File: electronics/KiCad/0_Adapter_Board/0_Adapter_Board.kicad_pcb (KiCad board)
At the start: 2 copper layers, 70 x 50 mm, 19 parts, among them J1 Conn_01x10, J2 Conn_01x10, J3 Conn_01x04, J4 Conn_01x04, J5 Conn_01x03, M1 MountingHole_3.2mm_M3_ISO7380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

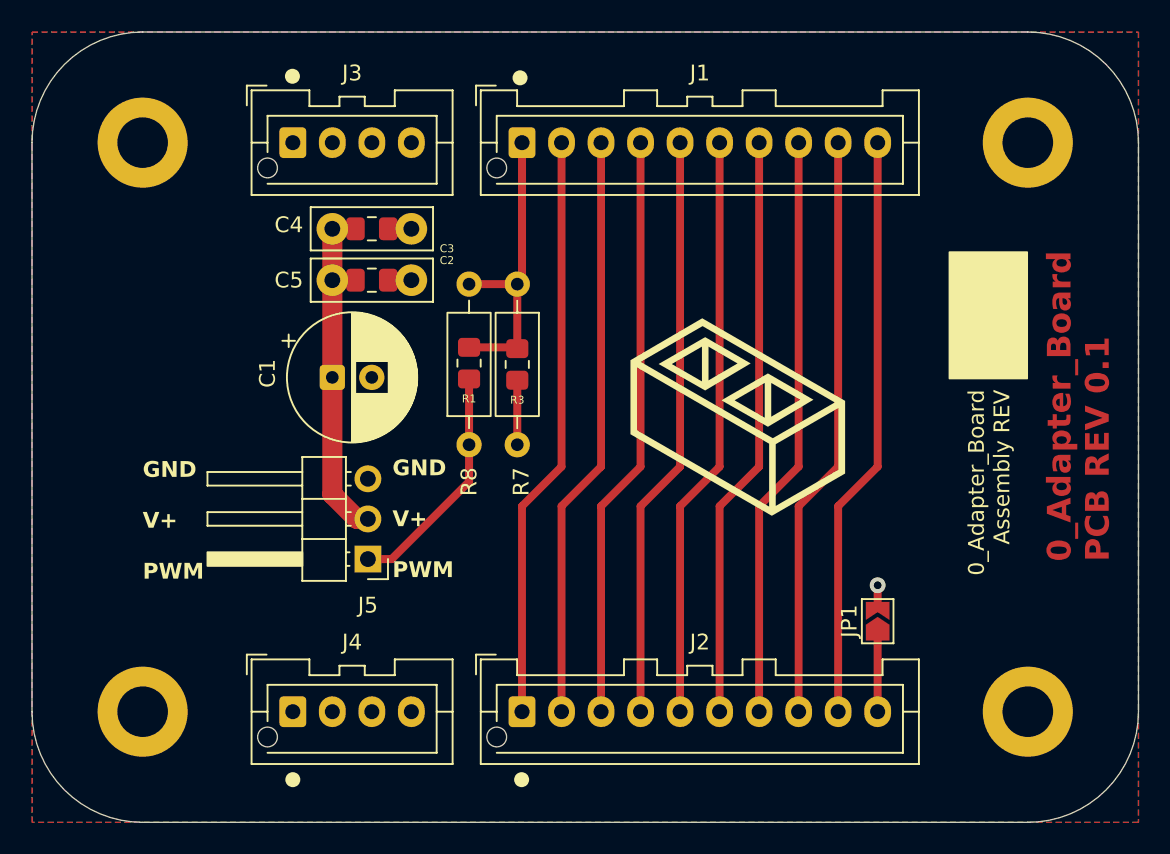
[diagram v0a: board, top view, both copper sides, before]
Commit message: Merge board v1.3 into main (clean-clone fixups, generated files trimmed to main level) (#289)
* Initial start to updates

Removed motor pages, updated Q2,Q3, Cleaned up power module connections.

- Still need to correct routing for these updates.

* PCA Update

Updated PCA to have level shifter for I2C lines and external oscillator for precision. Corrected Power to pull from 12V.

* Removed old circuits from PCB

Removed all unused traces

* Mid work update

Lots of rework on the SCH and PCB. Checkpoint.

* Updated with more layout

Compelted PCA on board.

* adding libraries

* REV0.9 for review

Took care of all open items on the electronics PCB except for the driver resistor addresses.

* Updates Just prior to Ordering V1.0 PCBs

Updates Just prior to Ordering V1.0 PCBs

* Updates to push to V1.0

Updates to push to V1.0

* Updates to push to V1.0 missing saves. . .

Updates to push to V1.0 missing saves. . .

* Correcting Part rotation for JLCPCB

Several parts needed the "FT Rotation Offset" parameter added to correct for part orientation for JLCPCB order.

* All orientations corrected

* latest update

* Updated to reflect V1.0 of layer board as well

Updated for initial orders with PCA module populated. Also updated to layer boards for flex cables.

* Updated data and notes

* Corrected SCH for power sequence issue

5V to Vsys for all powered items.
Correction of the PCA9306 power pins.
Added decoupling to oscillator and PCA9306.

* Updated for changes to the SCH items

Updated PCB to include all changed from the SCH.

* Updated rules to correct errors

Cleaned up rules a bit to prevent false errors.

* Started work on silk update

Slowly started work on silk update.

* Corrected the 10k to 1k for connecting resistors

R1 got fixed for the correct 1k instead of 10k for UART1

* Updated Silk on PCB

Added notes for describing the pins better in the silk layer.

* Updated REV to 1.3 to reflect changes

* Updated with Version 1.3

* KiCad: make the v1.3 project 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
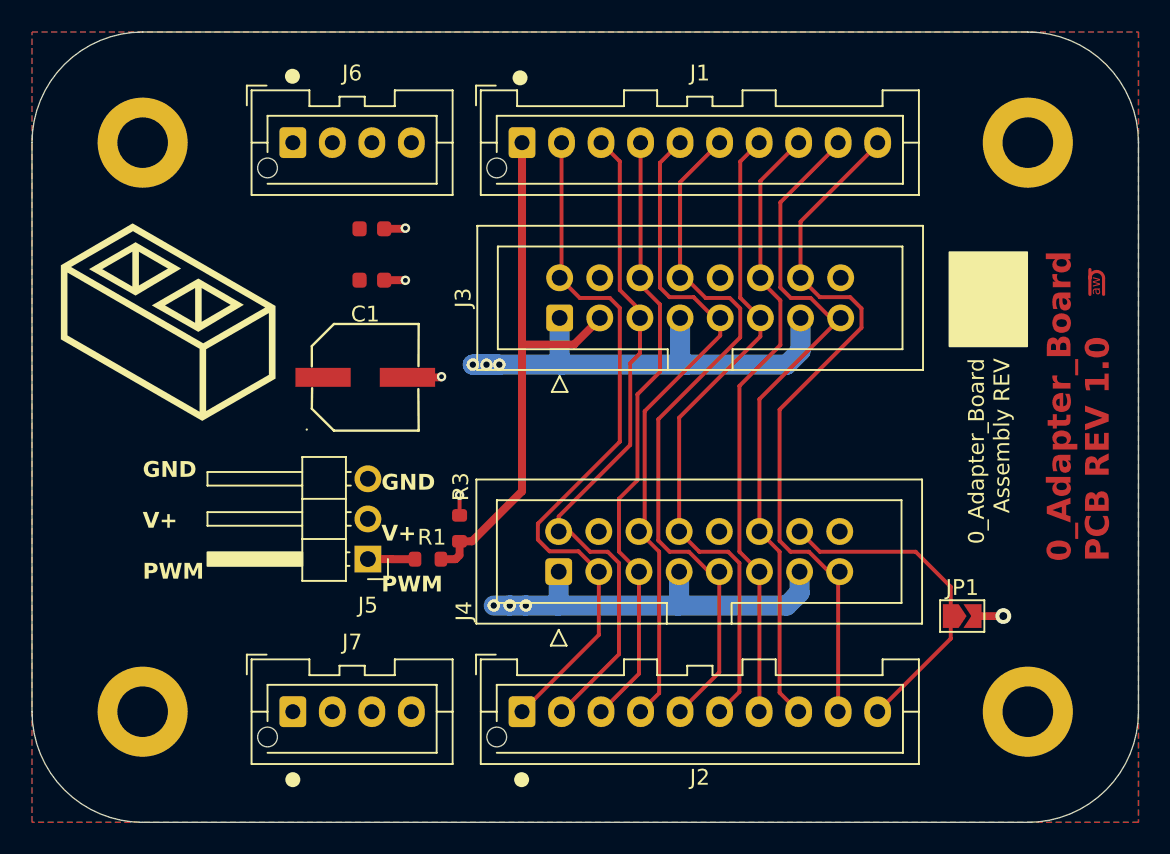
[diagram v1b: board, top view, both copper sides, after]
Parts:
- removed C4: 0.1uF, Capacitor_THT:C_Disc_D7.5mm_W2.5mm_P5.00mm
- removed C5: 1uF, Capacitor_THT:C_Disc_D7.5mm_W2.5mm_P5.00mm
- removed R7: 10k, Resistor_THT:R_Axial_DIN0207_L6.3mm_D2.5mm_P10.16mm_Horizontal
- removed R8: 0, Resistor_THT:R_Axial_DIN0207_L6.3mm_D2.5mm_P10.16mm_Horizontal
- added J6: Conn_01x04, Connector_JST:JST_XA_B04B-XASK-1-A_1x04_P2.50mm_Vertical, F.Cu at (76.5, 57.0)
- added J7: Conn_01x04, Connector_JST:JST_XA_B04B-XASK-1-A_1x04_P2.50mm_Vertical, F.Cu at (76.5, 93.0)
- added JAW: Maker's Mark, JAW:JAW, F.Cu at (127.4, 65.9)
- C1: value Filter Cap -> 100uF; footprint Capacitor_THT:CP_Radial_D8.0mm_P2.50mm -> EasyEDA:CAP-SMD_BD6.3-L6.6-W6.6-LS7.4-FD
- C2: footprint Capacitor_SMD:C_0805_2012Metric_Pad1.18x1.45mm_HandSolder -> PCM_JLCPCB:C_0603
- C3: value 0.1uF -> 100nF; footprint Capacitor_SMD:C_0805_2012Metric_Pad1.18x1.45mm_HandSolder -> PCM_JLCPCB:C_0603
- J3, J4: value Conn_01x04 -> Conn_02x08_Odd_Even; footprint Connector_JST:JST_XA_B04B-XASK-1-A_1x04_P2.50mm_Vertical -> Connector_IDC:IDC-Header_2x08_P2.54mm_Vertical
- R1: value 0 -> 0Ω; footprint Resistor_SMD:R_0805_2012Metric_Pad1.20x1.40mm_HandSolder -> PCM_JLCPCB:R_0603
- R3: value 10k -> 10kΩ; footprint Resistor_SMD:R_0805_2012Metric_Pad1.20x1.40mm_HandSolder -> PCM_JLCPCB:R_0603
- moved J3 20.2 mm to (93.4, 68.1), turned to 90 degrees
- moved J4 19.0 mm to (93.3, 84.1), turned to 90 degrees
- moved R1 12.7 mm to (85.0, 83.3), turned to 180 degrees
- moved R3 11.0 mm to (87.0, 81.4), turned to 90 degrees
- moved JP1 5.36 mm to (118.8, 87.0), turned to 0 degrees
- moved C2 3.25 mm to (81.5, 62.5)
- moved C3 3.25 mm to (81.5, 65.7)
- moved C1 2.08 mm to (81.1, 71.8)
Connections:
- C1 pad 1: +5V -> +ServoV
- C2 pad 1: +5V -> +ServoV
- C3 pad 1: +5V -> +ServoV
- J1 pad 1: /PWM_Signal -> /PWM_0
- J1 pad 10: Net-(J1-Pin_10) -> /PWM_9
- J1 pad 2: Net-(J1-Pin_2) -> /PWM_1
- J1 pad 3: Net-(J1-Pin_3) -> /PWM_2
- J1 pad 4: Net-(J1-Pin_4) -> /PWM_3
- J1 pad 5: Net-(J1-Pin_5) -> /PWM_4
- J1 pad 6: Net-(J1-Pin_6) -> /PWM_5
- J1 pad 7: Net-(J1-Pin_7) -> /PWM_6
- J1 pad 8: Net-(J1-Pin_8) -> /PWM_7
- J1 pad 9: Net-(J1-Pin_9) -> /PWM_8
- J2 pad 1: Net-(J1-Pin_2) -> /PWM_1
- J2 pad 10: Net-(J2-Pin_10) -> /Dead_Pin
- J2 pad 2: Net-(J1-Pin_3) -> /PWM_2
- J2 pad 3: Net-(J1-Pin_4) -> /PWM_3
- J2 pad 4: Net-(J1-Pin_5) -> /PWM_4
- J2 pad 5: Net-(J1-Pin_6) -> /PWM_5
- J2 pad 6: Net-(J1-Pin_7) -> /PWM_6
- J2 pad 7: Net-(J1-Pin_8) -> /PWM_7
- J2 pad 8: Net-(J1-Pin_9) -> /PWM_8
- J2 pad 9: Net-(J1-Pin_10) -> /PWM_9
- J3 pad 1: +5V -> +ServoV
- J3 pad 2: +5V -> /PWM_1
- J3 pad 3: GND -> /PWM_0
- J4 pad 1: +5V -> +ServoV
- J4 pad 2: +5V -> /PWM_2
- J4 pad 3: GND -> /PWM_1
- J5 pad 1: /Pin1_J5 -> /PWM_Signal
- J5 pad 2: +5V -> +ServoV
- JP1 pad 1: Net-(J2-Pin_10) -> /Dead_Pin
- R1 pad 1: /Pin1_J5 -> /PWM_0
- R3 pad 1: /PWM_Signal -> /PWM_0
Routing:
- net +ServoV: track 0.00 -> 57.2 mm, vias 0 -> 6
- net /PWM_9: track 0.00 -> 45.6 mm
- net /PWM_5: track 0.00 -> 45.6 mm
- net /PWM_1: track 0.00 -> 45.6 mm
- net /PWM_8: track 0.00 -> 43.4 mm
- net /PWM_2: track 0.00 -> 43.3 mm
- net /PWM_4: track 0.00 -> 42.4 mm
- net /PWM_6: track 0.00 -> 42.3 mm
- net /PWM_3: track 0.00 -> 39.1 mm
- net /PWM_7: track 0.00 -> 39.1 mm
- net Net-(J1-Pin_9): track 37.0 -> 0.00 mm
- net Net-(J1-Pin_8): track 37.0 -> 0.00 mm
- net Net-(J1-Pin_7): track 37.0 -> 0.00 mm
- net Net-(J1-Pin_6): track 37.0 -> 0.00 mm
- net Net-(J1-Pin_5): track 37.0 -> 0.00 mm
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- added copper zone on F.Cu, net +ServoV
- removed copper zone on F.Cu, net +5V
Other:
- board text added: "0_Adapter_Board PCB REV 1.0"
- board text removed: "0_Adapter_Board PCB REV 0.1"

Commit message: Add stencil tooling holes and PNP fiducials to adapter board, rev 1.0-pnp1
Same treatment as the distribution board: 4x 1.5mm NPTH holes (H1-H4)
near the corners for stencil printer pins and 3x 1mm/3mm-mask fiducials
(FID1-3) with extra clearance from pads and holes. Fixed fp-lib-table
EasyEDA URI from an absolute Windows path to ${KIPRJMOD}-relative.
Gerbers verified semantically identical to V1.0 apart from the added
features; BOM unchanged. DRC clean.

Co-Authored-By: Claude Fable 5 <noreply@anthropic.com>
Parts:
- added FID1: Fiducial_1mm_Mask3mm, Fiducial_1mm_Mask3mm, F.Cu at (62.5, 76.8)
- added FID2: Fiducial_1mm_Mask3mm, Fiducial_1mm_Mask3mm, F.Cu at (127.5, 62.5)
- added FID3: Fiducial_1mm_Mask3mm, Fiducial_1mm_Mask3mm, F.Cu at (127.5, 87.5)
- added H1: ToolingHole_1.5mm, EasyEDA:ToolingHole_1.5mm, F.Cu at (62.5, 55.5)
- added H2: ToolingHole_1.5mm, EasyEDA:ToolingHole_1.5mm, F.Cu at (124.5, 52.5)
- added H3: ToolingHole_1.5mm, EasyEDA:ToolingHole_1.5mm, F.Cu at (62.5, 94.5)
- added H4: ToolingHole_1.5mm, EasyEDA:ToolingHole_1.5mm, F.Cu at (124.5, 97.5)
